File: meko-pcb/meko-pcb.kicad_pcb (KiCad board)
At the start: 4 copper layers, 37 x 69 mm, 215 parts, among them IC2 TPS7A2033PDBVR, IC4 TAD5212IRGER, IC5 AS5600-ASOM, J1 USB_C_Receptacle_USB2.0_16P, J3 GDEY0154D67, J4 Conn_ARM_SWD_TagConnect_TC203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, J5 503398-1892, Q1 SS8050, Q2 Si1308EDL, SW1 SW_Push, SW2 SW_Push, SW3 SW_Push, SW4 SW_Push, SW5 SW_Push, SW6 SW_Push, SW7 SW_Push, SW9 SW_Push, U1 nPM1300-QEXX, U2 nRF5340-QKxx, Y1 32MHz, Y2 32.768 kHz

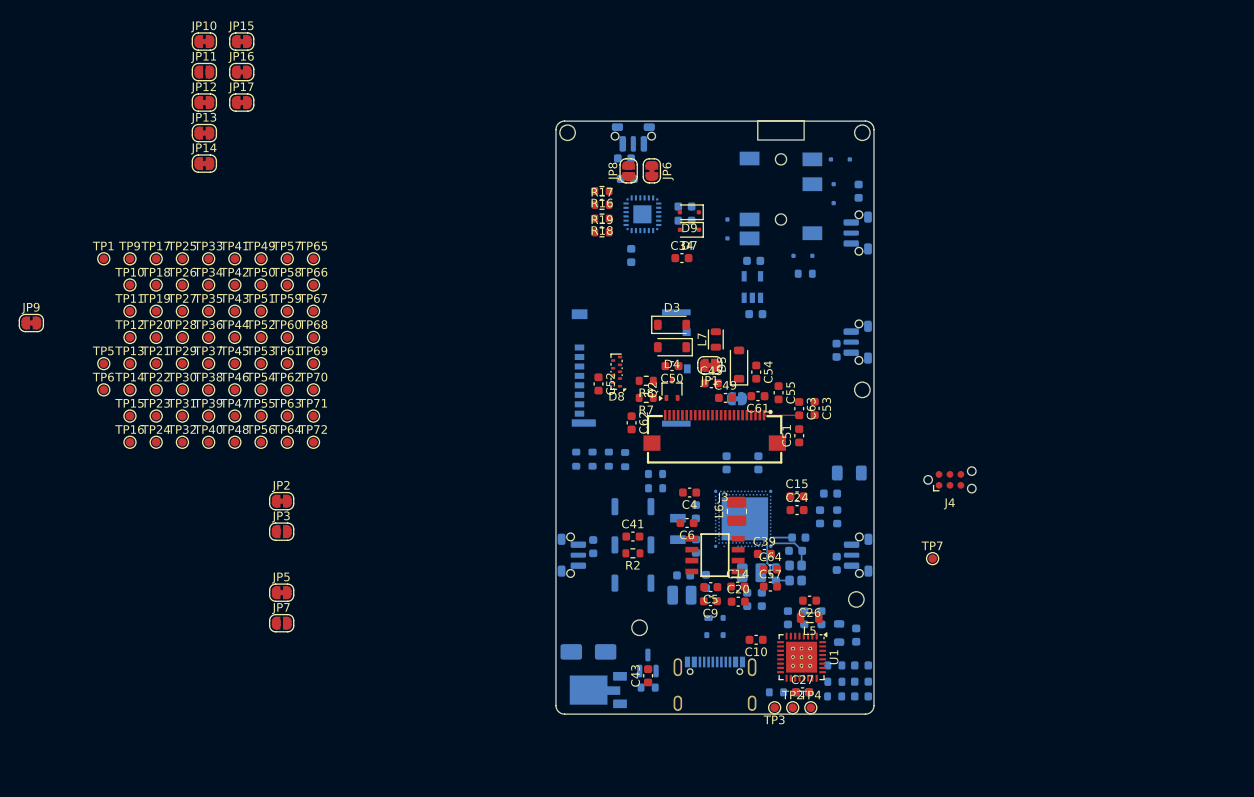
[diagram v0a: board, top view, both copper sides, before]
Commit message: removed caps from software controlled buttons, placed jumpers
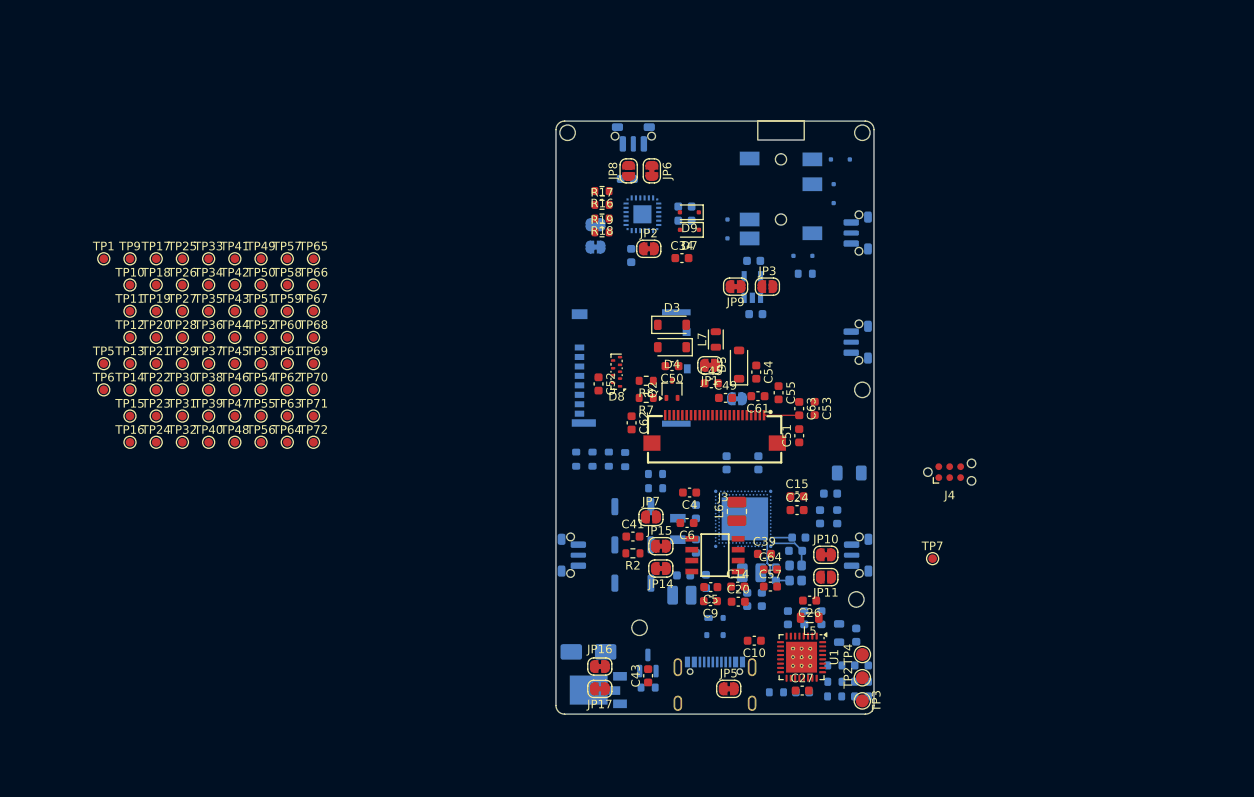
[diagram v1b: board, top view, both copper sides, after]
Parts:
- removed C29, C33, C36, C38, C40: 100nF, Capacitor_SMD:C_0603_1608Metric
- JP12, JP13: moved to B.Cu
- TP2, TP3, TP4: footprint TestPoint:TestPoint_Pad_D1.0mm -> TestPoint:TestPoint_Pad_D1.5mm
- moved JP10 93.8 mm to (107.7, 71.5)
- moved JP11 93.2 mm to (107.7, 74.1), turned to 180 degrees
- moved JP9 82.0 mm to (97.2, 40.3), turned to 180 degrees
- moved JP16 80.7 mm to (81.4, 84.5), turned to 180 degrees
- moved JP17 79.9 mm to (81.4, 87.1), turned to 180 degrees
- moved JP15 76.3 mm to (88.5, 70.5), turned to 180 degrees
- moved JP14 71.0 mm to (88.5, 73.1), turned to 180 degrees
- moved JP3 63.3 mm to (100.9, 40.3)
- moved JP5 53.2 mm to (96.4, 87.1)
- moved JP2 51.8 mm to (87.1, 35.9)
- moved JP12 48.5 mm to (80.9, 35.7)
- moved JP13 46.7 mm to (80.9, 33.1), turned to 180 degrees
- moved JP7 44.7 mm to (87.3, 67.1)
- moved TP3 10.2 mm to (111.9, 88.5), turned to -90 degrees
- moved TP2 8.82 mm to (111.9, 85.8), turned to 90 degrees
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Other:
- copper layers 4 -> 6

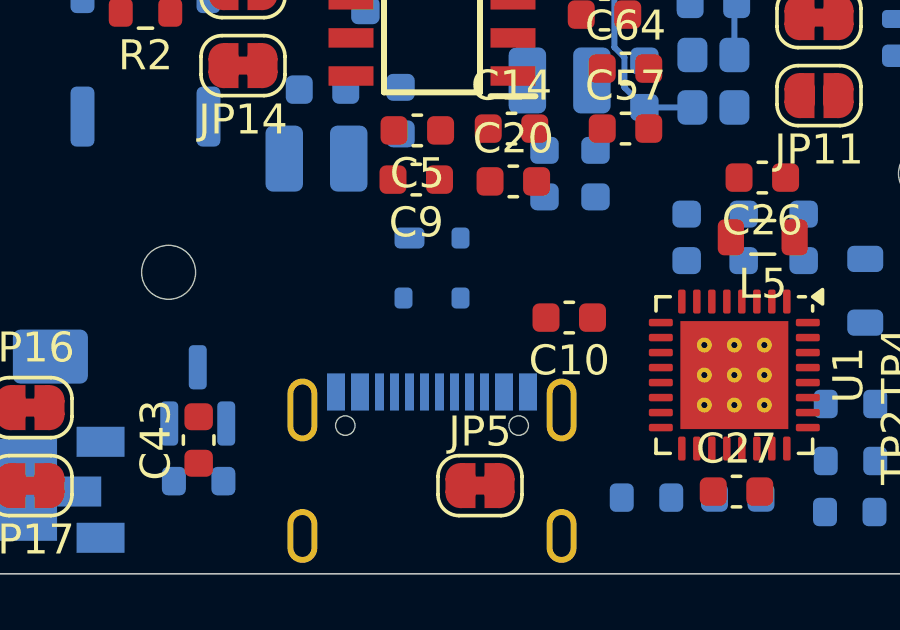
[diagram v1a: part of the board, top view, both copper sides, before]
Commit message: made schematic prettier
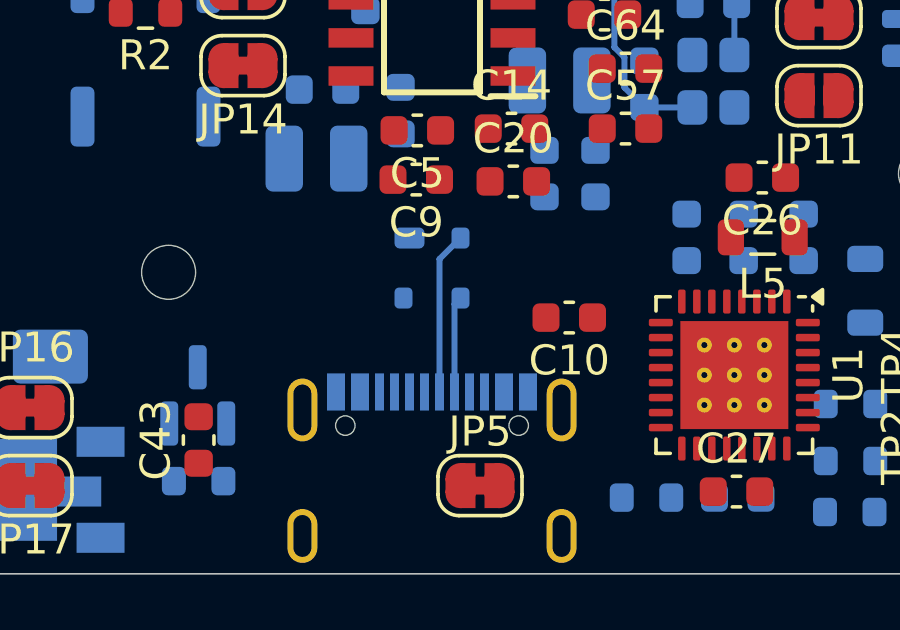
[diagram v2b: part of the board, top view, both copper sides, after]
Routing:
- net /D+: track 0.00 -> 5.42 mm
- net /D-: track 0.00 -> 3.21 mm
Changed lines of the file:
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@@
+	)
+	(segment
+		(start 95.05 79.5)
+		(end 95.75 78.8)
+		(width 0.2)
+		(layer "B.Cu")
+		(net 51)
+	)
+	(segment
+		(start 95.05 83.93125)
+		(end 95.05 79.5)
+		(width 0.2)
+		(layer "B.Cu")
+		(net 51)
+	)
+	(segment
+		(start 95.55 83.93125)
+		(end 95.55 81)
+		(width 0.2)
+		(layer "B.Cu")
+		(net 52)
+	)
+	(segment
+		(start 95.55 81)
+		(end 95.75 80.8)
+		(width 0.2)
+		(layer "B.Cu")
+		(net 52)
 	)
 	(segment

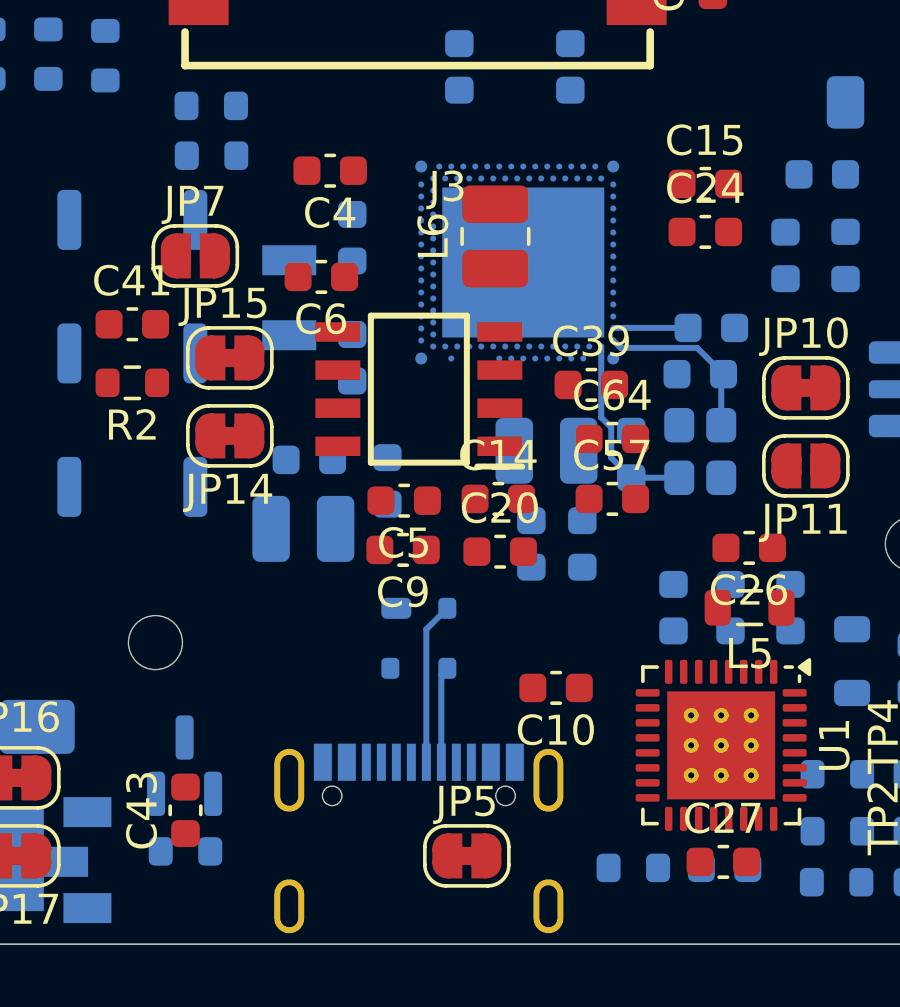
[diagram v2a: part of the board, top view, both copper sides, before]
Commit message: routed some traces
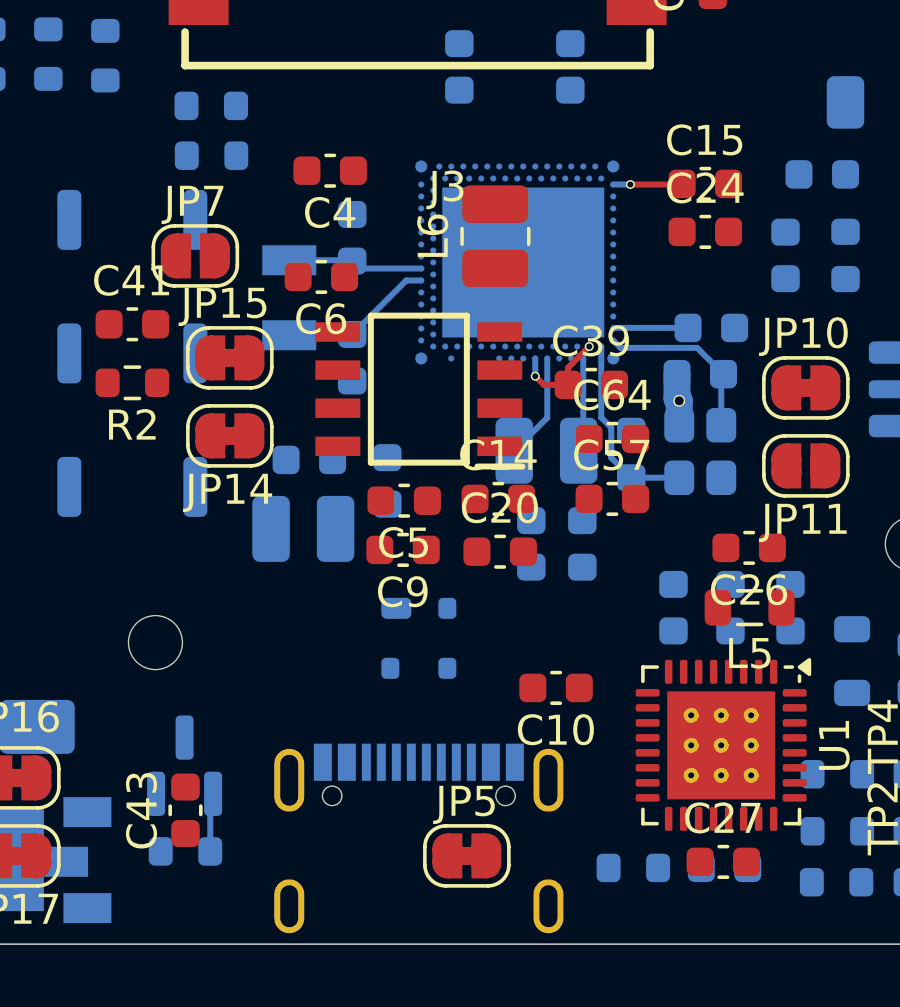
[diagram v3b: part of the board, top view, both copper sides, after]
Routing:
- net +3V3: track 2.50 -> 8.46 mm, vias 0 -> 3
- net /D+: track 5.42 -> 0.00 mm
- net /XL1: track 0.00 -> 5.16 mm
- net /XL2: track 0.00 -> 4.51 mm
- net Net-(U2-DCC): track 0.00 -> 3.53 mm
- net /D-: track 3.21 -> 0.00 mm
- net Net-(U2-DECR): track 0.00 -> 3.14 mm
- net Net-(Q1-B): track 0.00 -> 1.96 mm
- net GND: track 0.00 -> 1.73 mm, vias 0 -> 1
- added copper zone on In1.Cu, net GND
- added copper zone on In3.Cu, net GND
- added copper zone on In4.Cu, net GND

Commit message: routed a bunch of traces
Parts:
- C43, JP16, JP17: moved to B.Cu
- moved TP25 41.3 mm to (36.5, 78.1)
- moved TP65 41.1 mm to (48.7, 78.1)
- moved TP35 35.2 mm to (39.5, 78.1)
- moved TP33 35.2 mm to (39.5, 72.0)
- moved TP34 35.2 mm to (39.5, 75.1)
- moved TP45 29.1 mm to (42.6, 78.1)
- moved TP41 29.1 mm to (42.6, 65.9)
- moved TP42 29.1 mm to (42.6, 69.0)
- moved TP43 29.1 mm to (42.6, 72.0)
- moved TP44 29.1 mm to (42.6, 75.1)
- moved TP11 23.8 mm to (33.4, 65.9)
- moved TP15 23.8 mm to (33.4, 78.1)
- moved TP10 23.8 mm to (33.4, 62.9)
- moved TP12 23.8 mm to (33.4, 69.0)
- moved TP13 23.8 mm to (33.4, 72.0)
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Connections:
- net +HALL3V3 renamed +3V3HALL
- D8 pad 1: /MEM_COM -> /MEM_SWITCH
- D8 pad 4: unconnected-(D8-Line-6-Pad4) -> /MEM_LEVER
- TP20 pad 1: /DISPL_RESET -> /PMIC_GPIO2
- TP24 pad 1: Net-(U2-DCX/TRACECLK/P0.12) -> /DISPL_RESET
- TP25 pad 1: /BTN_SIDE_R -> /DISPL_BUSY
- TP26 pad 1: /BTN_SIDE_L -> /DISPL_~{D/C}
- TP27 pad 1: /PMIC_GPIO0 -> /DISPL_SCL
- TP28 pad 1: /PMIC_GPIO1 -> /DISPL_~{CS}
- TP29 pad 1: /PMIC_GPIO2 -> /DISPL_SDA
- TP30 pad 1: /PMIC_GPIO3 -> /BTN_SIDE_R
- TP32 pad 1: /DISPL_SCL -> /BTN_SIDE_L
- TP33 pad 1: /DISPL_SDA -> Net-(U2-P0.21)
- TP38 pad 1: Net-(U2-AIN5/P0.26) -> /BTN_PWR
- TP39 pad 1: /PMIC_GPIO4 -> /MEM_LEVER
- TP44 pad 1: /BTN_PWR -> /MEM_SWITCH
- TP47 pad 1: /DISPL_~{D/C} -> Net-(U2-P1.04)
- TP49 pad 1: /DISPL_BUSY -> /PMIC_GPIO0
- TP50 pad 1: Net-(U2-P1.07) -> /PMIC_GPIO1
- TP51 pad 1: /DISPL_~{CS} -> Net-(U2-P1.08)
- TP54 pad 1: Net-(U2-P1.11) -> /PMIC_GPIO3
- TP55 pad 1: /MEM_LEVER -> /PMIC_GPIO4
- TP56 pad 1: /MEM_SWITCH -> Net-(U2-P1.14)
- U2 pad A17: /MEM_LEVER -> /PMIC_GPIO4
- U2 pad AK10: /PMIC_GPIO0 -> /DISPL_SCL
- U2 pad AK12: /PMIC_GPIO2 -> /DISPL_SDA
- U2 pad AK14: /PMIC_GPIO3 -> /BTN_SIDE_R
- U2 pad AK16: /DISPL_SCL -> /BTN_SIDE_L
- U2 pad AK24: Net-(U2-P1.07) -> /PMIC_GPIO1
- U2 pad AK30: /PMIC_GPIO4 -> /MEM_LEVER
- U2 pad AK6: Net-(U2-DCX/TRACECLK/P0.12) -> /DISPL_RESET
- U2 pad AK8: /BTN_SIDE_L -> /DISPL_~{D/C}
- U2 pad AL15: /DISPL_SDA -> Net-(U2-P0.21)
- U2 pad AL19: /DISPL_~{D/C} -> Net-(U2-P1.04)
- U2 pad AL21: /DISPL_BUSY -> /PMIC_GPIO0
- U2 pad AL23: /DISPL_~{CS} -> Net-(U2-P1.08)
- U2 pad AL29: Net-(U2-AIN5/P0.26) -> /BTN_PWR
- U2 pad AL5: /BTN_SIDE_R -> /DISPL_BUSY
- U2 pad AL9: /PMIC_GPIO1 -> /DISPL_~{CS}
- U2 pad B16: /MEM_SWITCH -> Net-(U2-P1.14)
- U2 pad B18: /DISPL_RESET -> /PMIC_GPIO2
- U2 pad B20: Net-(U2-P1.11) -> /PMIC_GPIO3
- U2 pad P2: /BTN_PWR -> /MEM_SWITCH
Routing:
- net /MEM_CS: track 0.00 -> 34.0 mm, vias 0 -> 5
- net /MEM_MOSI: track 0.00 -> 33.6 mm, vias 0 -> 5
- net /MEM_SCK: track 0.00 -> 32.4 mm, vias 0 -> 5
- net /MEM_MISO: track 0.00 -> 31.5 mm, vias 0 -> 5
- net REG-OUT: track 0.00 -> 28.3 mm, vias 0 -> 4
- net /OUT_R: track 0.00 -> 21.3 mm
- net /DISPL_PREVGL: track 0.00 -> 21.2 mm
- net VBUSIN: track 0.00 -> 20.6 mm, vias 0 -> 4
- net /D+: track 0.00 -> 15.0 mm
- net /D-: track 0.00 -> 15.0 mm
- net Net-(D2-A): track 0.00 -> 14.4 mm
- net Net-(D5-A): track 0.00 -> 14.0 mm
- net +3V3: track 8.46 -> 21.8 mm, vias 3 -> 7
- net /AUDIO_TN: track 0.00 -> 12.3 mm
- net /OUT_L: track 0.00 -> 11.1 mm
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
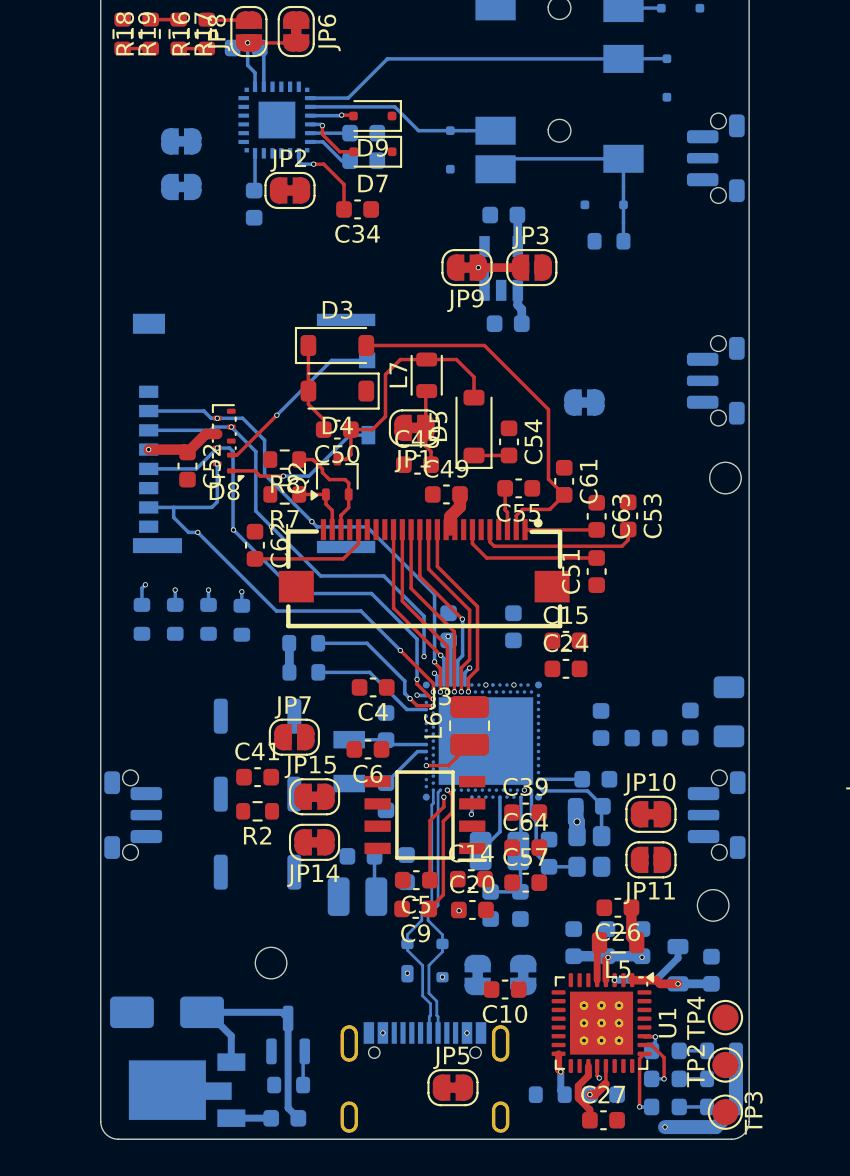
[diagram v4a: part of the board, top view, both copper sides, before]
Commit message: routed more traces
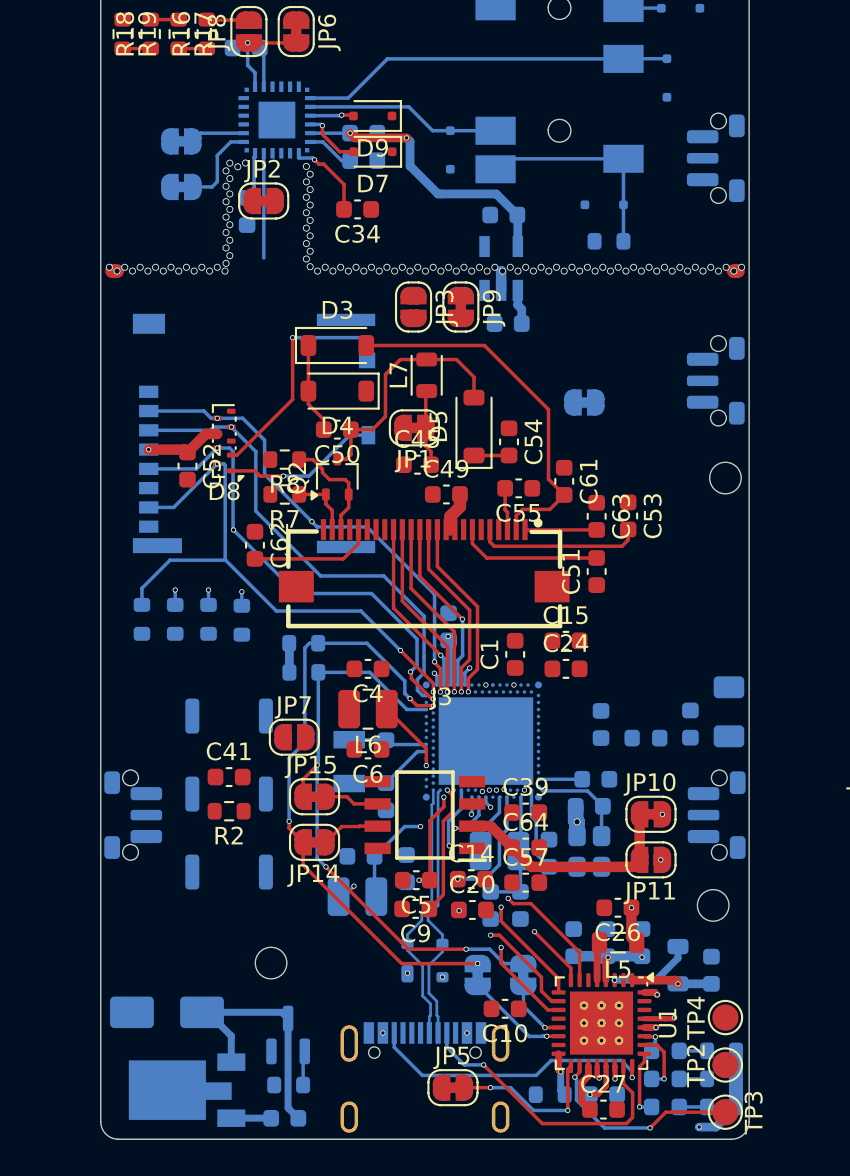
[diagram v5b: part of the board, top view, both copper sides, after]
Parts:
- C1: moved to F.Cu
- moved JP3 7.12 mm to (94.2, 42.5), turned to -90 degrees
- moved L6 5.88 mm to (91.5, 65.5), turned to 180 degrees
- moved JP9 2.28 mm to (96.8, 42.5), turned to -90 degrees
- moved C41 1.63 mm to (83.6, 69.3)
- moved R2 1.63 mm to (83.6, 71.3)
- moved SW1 1.63 mm to (83.6, 65.8)
- moved SW7 1.63 mm to (83.6, 70.3)
- moved SW9 1.63 mm to (83.6, 74.7)
- moved JP2 1.62 mm to (85.6, 36.5)
- moved C1 1.58 mm to (100.0, 62.3)
- moved C4 1.10 mm to (91.5, 63.2)
- moved C10 1.10 mm to (99.4, 82.6)
- moved C27 0.61 mm to (105.0, 88.3)
- moved C44 0.58 mm to (84.7, 37.1)
- turned JP13 to 0 degrees
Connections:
- net Net-(IC5-VDD3V3) renamed /HALLVDD
- TP42 pad 1: /AUDIO_GPO1 -> /AUDIO_GPI1
- TP43 pad 1: /AUDIO_GPI1 -> /PMIC_GPIO1
- TP47 pad 1: Net-(U2-P1.04) -> /AUDIO_GPO1
- TP49 pad 1: /PMIC_GPIO0 -> Net-(U2-P1.06)
- TP50 pad 1: /PMIC_GPIO1 -> Net-(U2-P1.07)
- TP54 pad 1: /PMIC_GPIO3 -> /PMIC_GPIO0
- TP56 pad 1: Net-(U2-P1.14) -> /PMIC_GPIO3
- U2 pad AK24: /PMIC_GPIO1 -> Net-(U2-P1.07)
- U2 pad AL19: Net-(U2-P1.04) -> /AUDIO_GPO1
- U2 pad AL21: /PMIC_GPIO0 -> Net-(U2-P1.06)
- U2 pad B16: Net-(U2-P1.14) -> /PMIC_GPIO3
- U2 pad B20: /PMIC_GPIO3 -> /PMIC_GPIO0
- U2 pad B22: /AUDIO_GPI1 -> /PMIC_GPIO1
- U2 pad B24: /AUDIO_GPO1 -> /AUDIO_GPI1
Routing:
- net /I2C_SDA: track 7.04 -> 34.1 mm, vias 0 -> 3
- net /I2C_SCL: track 8.47 -> 34.7 mm, vias 2 -> 4
- net VBUS: track 5.07 -> 23.9 mm, vias 1 -> 3
- net /CC2: track 0.00 -> 16.7 mm, vias 0 -> 1
- net /CC1: track 0.00 -> 16.5 mm, vias 0 -> 1
- net +3V3HALL: track 0.00 -> 14.6 mm, vias 0 -> 2
- net /PMIC_GPIO3: track 0.00 -> 14.3 mm, vias 0 -> 2
- net /PMIC_GPIO4: track 0.00 -> 14.2 mm, vias 0 -> 2
- net /PMIC_GPIO0: track 0.00 -> 13.4 mm, vias 0 -> 2
- net /HALLVDD: track 0.00 -> 13.3 mm
- net /PMIC_GPIO2: track 0.00 -> 13.2 mm, vias 0 -> 2
- net /PMIC_GPIO1: track 0.00 -> 12.5 mm, vias 0 -> 2
- net +3V3: track 21.8 -> 34.1 mm, vias 7 -> 11
- net +3V3AVDD: track 4.08 -> 16.4 mm, vias 0 -> 2
- net /BATTHERM: track 0.00 -> 11.6 mm, vias 0 -> 2
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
